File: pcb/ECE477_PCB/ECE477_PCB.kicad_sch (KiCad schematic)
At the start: 65 parts, among them J1 ESC, J2 USB_B_Micro, J3 AUX_PWR, J4 DEBUG, J5 ELRS, M1 Brushed_DC, M2 Brushed_DC, M3 Brushed_DC, M4 Brushed_DC, Q1 IRLML6244TR, Q2 IRLML6244TR, Q3 IRLML6244TR, Q4 IRLML6244TR, SW1 RESET, U1 LM78L05_TO92, U2 LM1117-3.3, U3 FT230XQ, U4 STM32F446RETx, Y1 16MHz X322516MLB4SI

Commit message: modified layout of motor control and power, added minimal initial schematic for LiDAR and footprints
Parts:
- removed U1: LM78L05_TO92, Package_TO_SOT_THT:TO-92_Inline, symbol Regulator_Linear:LM78L05_TO92
- added C10, C12, C13, C14, C8, C9: 0.1uF, Capacitor_SMD:C_0603_1608Metric, symbol Device:C_Small
- added C16, C17: 1uF, Capacitor_SMD:C_0603_1608Metric, symbol Device:C_Small
- added C29: 33uF 35V, Capacitor_SMD:C_1206_3216Metric, symbol Device:C_Small
- added D4: 5V, LED_SMD:LED_0603_1608Metric, symbol Device:LED
- added H1, H2, H3, H4: MountingHole, MountingHole:MountingHole_3.2mm_M3, symbol Mechanical:MountingHole
- added J10: ToF 5, Connector_PinHeader_1.00mm:PinHeader_1x05_P1.00mm_Vertical, symbol Connector_Generic:Conn_01x05
- added J6: ToF 1, Connector_PinHeader_1.00mm:PinHeader_1x05_P1.00mm_Vertical, symbol Connector_Generic:Conn_01x05
- added J7: ToF 2, Connector_PinHeader_1.00mm:PinHeader_1x05_P1.00mm_Vertical, symbol Connector_Generic:Conn_01x05
- added J8: ToF 3, Connector_PinHeader_1.00mm:PinHeader_1x05_P1.00mm_Vertical, symbol Connector_Generic:Conn_01x05
- added J9: ToF 4, Connector_PinHeader_1.00mm:PinHeader_1x05_P1.00mm_Vertical, symbol Connector_Generic:Conn_01x05
- added R9: 4.7k, Resistor_SMD:R_0603_1608Metric, symbol Device:R
- added U2: Pololu_S13V10F5, Connector_PinHeader_2.54mm:PinHeader_1x03_P2.54mm_Horizontal, symbol Pololu_Regulator:Pololu_S13V10F5
- D3: renamed from D1; value LED -> 3.3V
- D5: renamed from D2; value LED -> ST
- J4: renamed from J5; footprint Connector_PinHeader_2.54mm:PinHeader_1x04_P2.54mm_Vertical -> Connector_PinHeader_1.27mm:PinHeader_1x04_P1.27mm_Vertical
- TP1: footprint TestPoint:TestPoint_THTPad_D1.5mm_Drill0.7mm -> TestPoint:TestPoint_Pad_D1.0mm
- TP2: footprint (none) -> TestPoint:TestPoint_Pad_D1.0mm
- U3: renamed from U2; value LM1117-3.3 -> REG1117-3.3; footprint (none) -> Package_TO_SOT_SMD:SOT-223
- renumbered C3 to C1, C19 to C11, C18 to C15, C22 to C18, C20 to C19, C6 to C2, C21 to C20, C1 to C21, C2 to C22, C8 to C23, C17 to C24, C4 to C3, C7 to C4, C9 to C6, C10 to C7, D7 to D1, D8 to D2, D3 to D6, D4 to D7, D5 to D8, D6 to D9, J4 to J1, J1 to J3, J3 to J5, R25 to R1, R8 to R10, R4 to R11, R18 to R12, R5 to R13, R1 to R14, R9 to R15, R11 to R16, R13 to R17, R3 to R18, R10 to R19, R15 to R2, R12 to R20, R14 to R21, R16 to R3, R2 to R4, R7 to R5, R19 to R6, R6 to R7, R17 to R8, U4 to U1, U3 to U4
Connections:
- net +10V: now also C29.1, U2.3 (VI)
- net +3V3: now also C15.2, C10.1, C12.2, C13.2, C14.2, C8.1, C9.1; no longer C15.1
- net +5V: now also C16.2, D4.2 (A), U2.1 (VO)
- net GND: now also C15.1, C10.2, C12.1, C13.1, C14.1, C16.1, C17.1, C29.2, C8.2, C9.2, J10.1 (Pin_1), J6.1 (Pin_1), J7.1 (Pin_1), J8.1 (Pin_1), J9.1 (Pin_1), R9.1, U2.2 (GND); no longer C15.2
- net NRST: now also C17.2
- new net: D4.1 (K), R9.2
- new net +3.3V: J10.2 (Pin_2), J6.2 (Pin_2), J7.2 (Pin_2), J8.2 (Pin_2), J9.2 (Pin_2)
- new net TOF_1_SHTDN: J6.5 (Pin_5)
- new net TOF_2_SHTDN: J7.5 (Pin_5)
- new net TOF_3_SHTDN: J8.5 (Pin_5)
- new net TOF_4_SHTDN: J9.5 (Pin_5)
- new net TOF_5_SHTDN: J10.5 (Pin_5)
- new net TOF_SCLK: J10.3 (Pin_3), J6.3 (Pin_3), J7.3 (Pin_3), J8.3 (Pin_3), J9.3 (Pin_3)
- new net TOF_SDA: J10.4 (Pin_4), J6.4 (Pin_4), J7.4 (Pin_4), J8.4 (Pin_4), J9.4 (Pin_4)
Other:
- removed sheet DataLogger
- moved on the sheet: C11, C15, D3, D5, R10, R11, R12, R13, R4, R5, R6

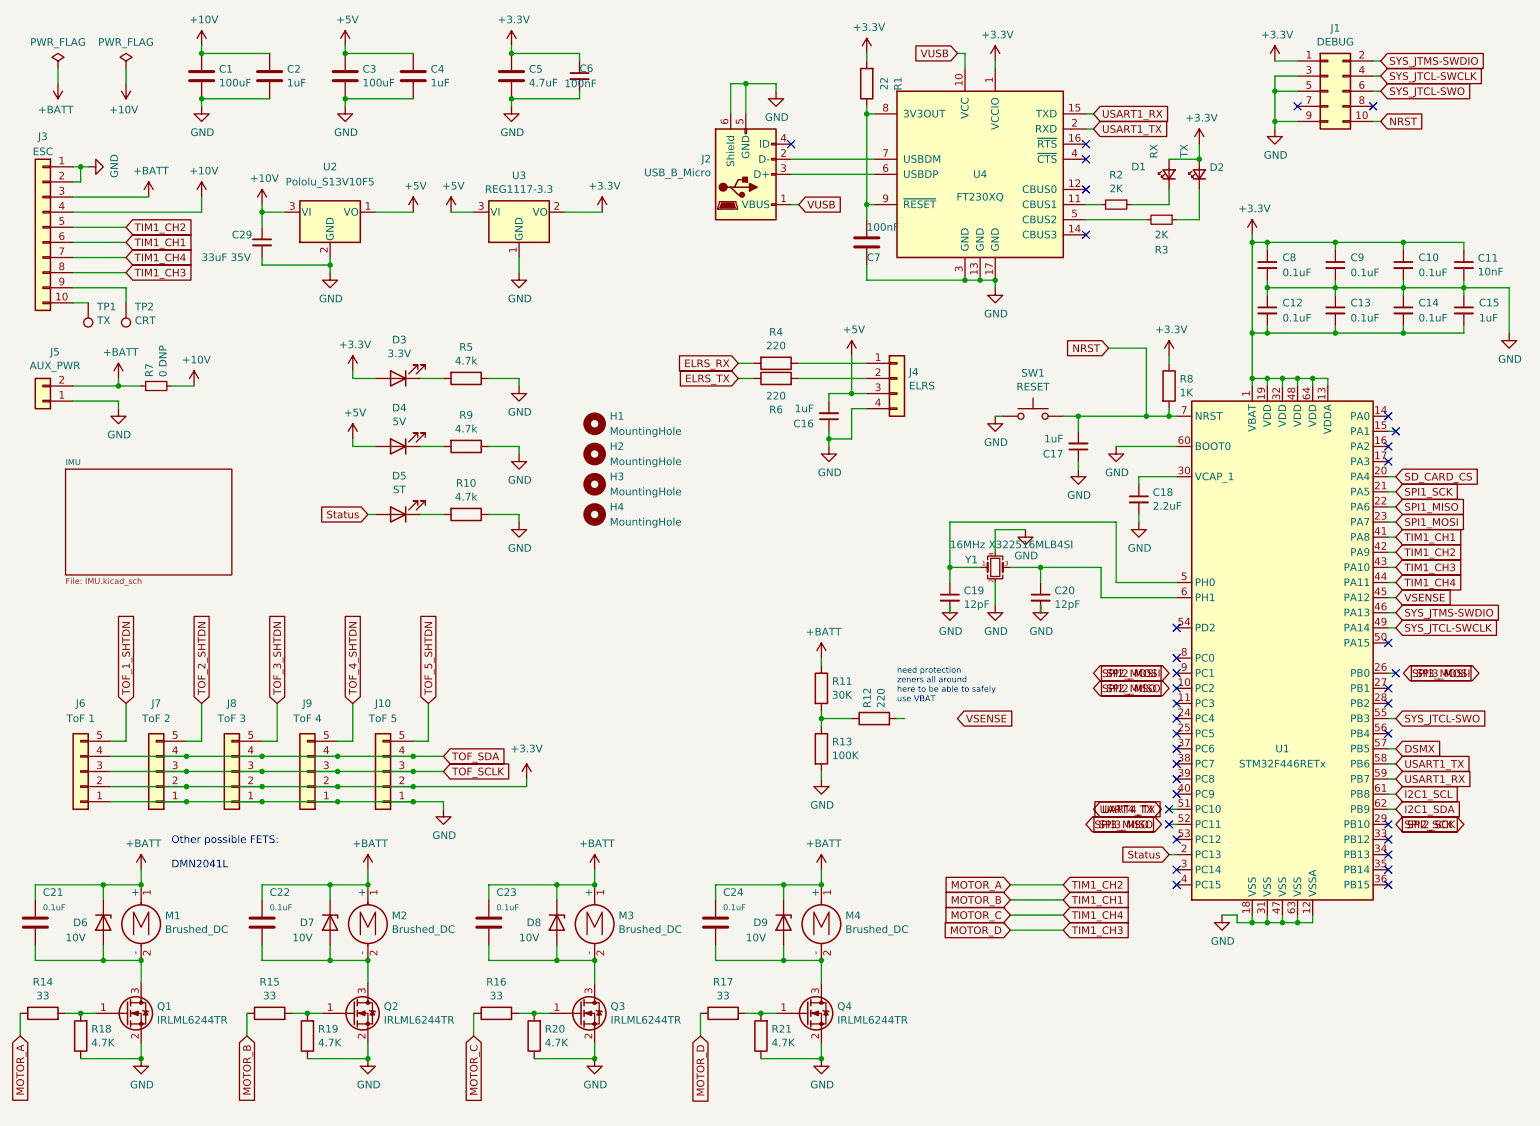
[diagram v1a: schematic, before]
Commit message: updated schematic I2C and UART connections
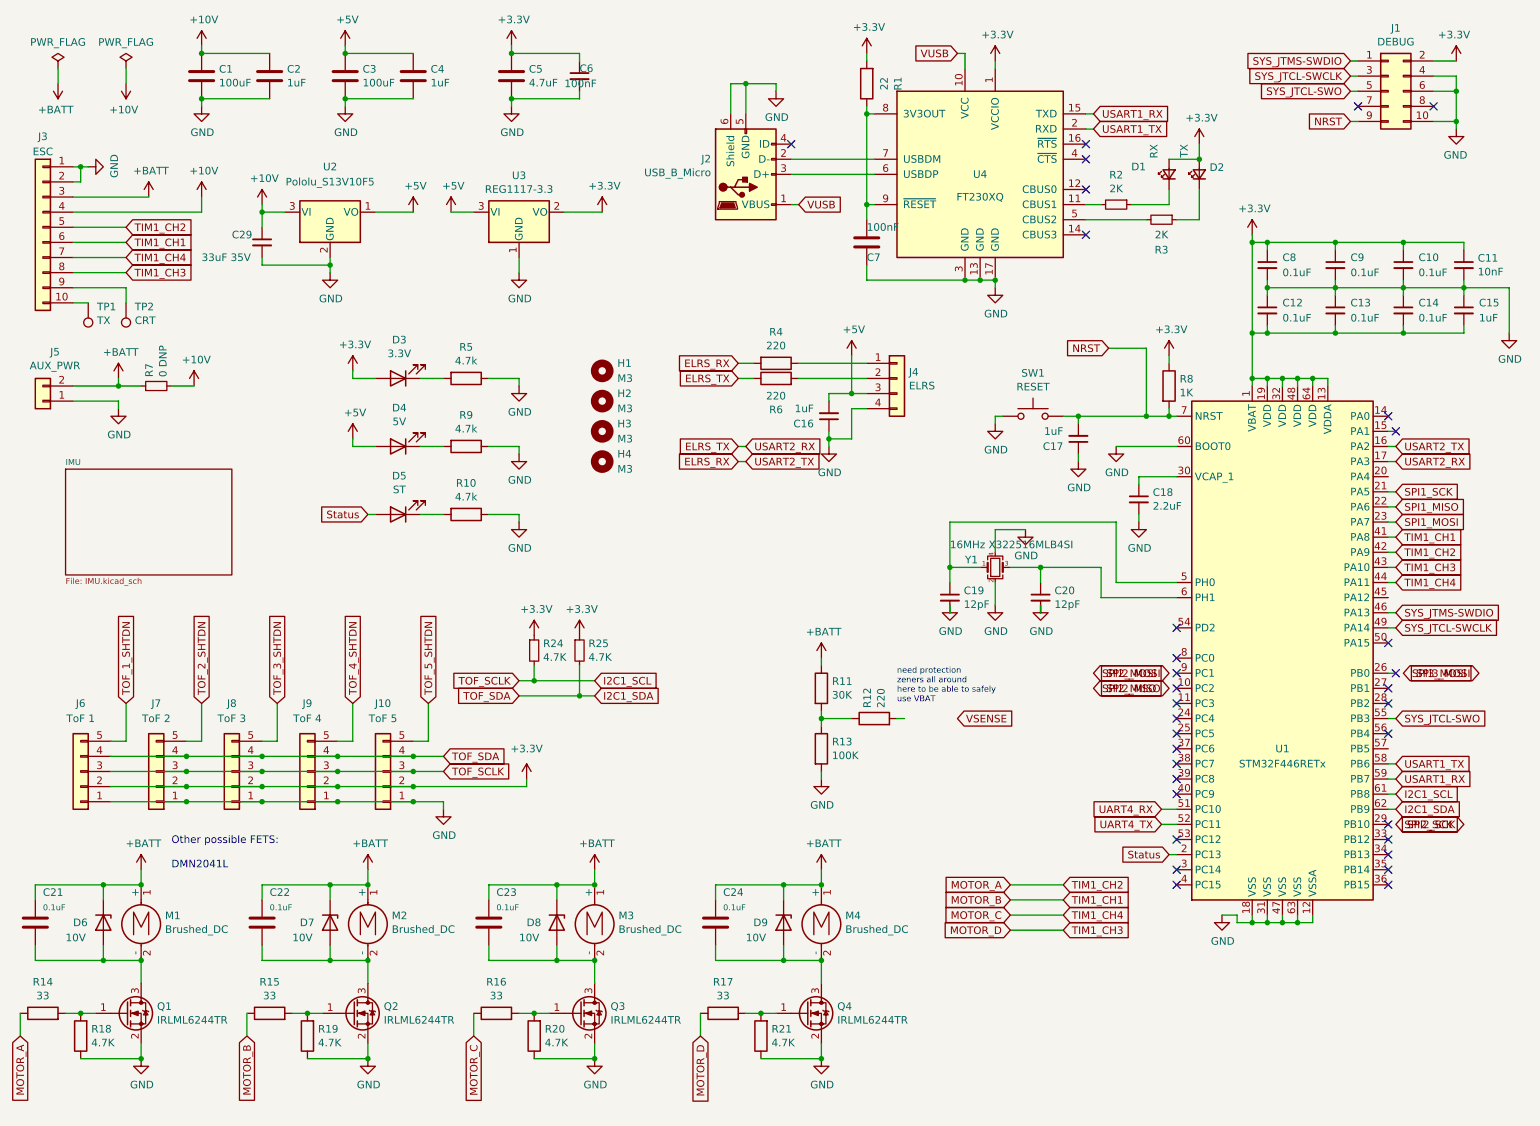
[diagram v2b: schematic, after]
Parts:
- added R24, R25: 4.7K, Resistor_SMD:R_0603_1608Metric, symbol Device:R_Small
- H1, H2, H3, H4: value MountingHole -> M3
- J2: footprint Connector_USB:USB_Micro-B_Molex_47346-0001 -> Connector_USB:USB_Micro-B_Molex-105017-0001
- J4: footprint Connector_PinHeader_1.27mm:PinHeader_1x04_P1.27mm_Vertical -> Connector_PinSocket_1.27mm:PinSocket_1x04_P1.27mm_Vertical
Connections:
- net TOF_SCLK is gone; now on net I2C1_SCL: J10.3 (Pin_3), J6.3 (Pin_3), J7.3 (Pin_3), J8.3 (Pin_3), J9.3 (Pin_3)
- net TOF_SDA is gone; now on net I2C1_SDA: J10.4 (Pin_4), J6.4 (Pin_4), J7.4 (Pin_4), J8.4 (Pin_4), J9.4 (Pin_4)
- net +3V3: now also J1.2 (Pin_2), R24.1, R25.1; no longer J1.1 (Pin_1)
- net ELRS_RX: now also U1.16 (PA2)
- net ELRS_TX: now also U1.17 (PA3)
- net GND: now also J1.10 (Pin_10), J1.4 (Pin_4), J1.6 (Pin_6); no longer J1.3 (Pin_3), J1.5 (Pin_5), J1.9 (Pin_9)
- net I2C1_SCL: now also R24.2
- net I2C1_SDA: now also R25.2
- net NRST: now also J1.9 (Pin_9); no longer J1.10 (Pin_10)
- net SYS_JTCL-SWCLK: now also J1.3 (Pin_3); no longer J1.4 (Pin_4)
- net SYS_JTCL-SWO: now also J1.5 (Pin_5); no longer J1.6 (Pin_6)
- net SYS_JTMS-SWDIO: now also J1.1 (Pin_1); no longer J1.2 (Pin_2)
- net UART4_TX: now also U1.52 (PC11)
- net VSENSE: no longer U1.45 (PA12)
- net UART4_RX: now reaches U1.51 (PC10)
- net DSMX: no longer names the net of U1.57 (PB5)
- net SD_CARD_CS: no longer names the net of U1.20 (PA4)
- no-connect marks 37 -> 33
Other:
- moved on the sheet: C17, H1, H2, H3, H4, J1

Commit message: getting pretty close. fixed DRC errors, moved UARTS and radio connector, added pi zero connector
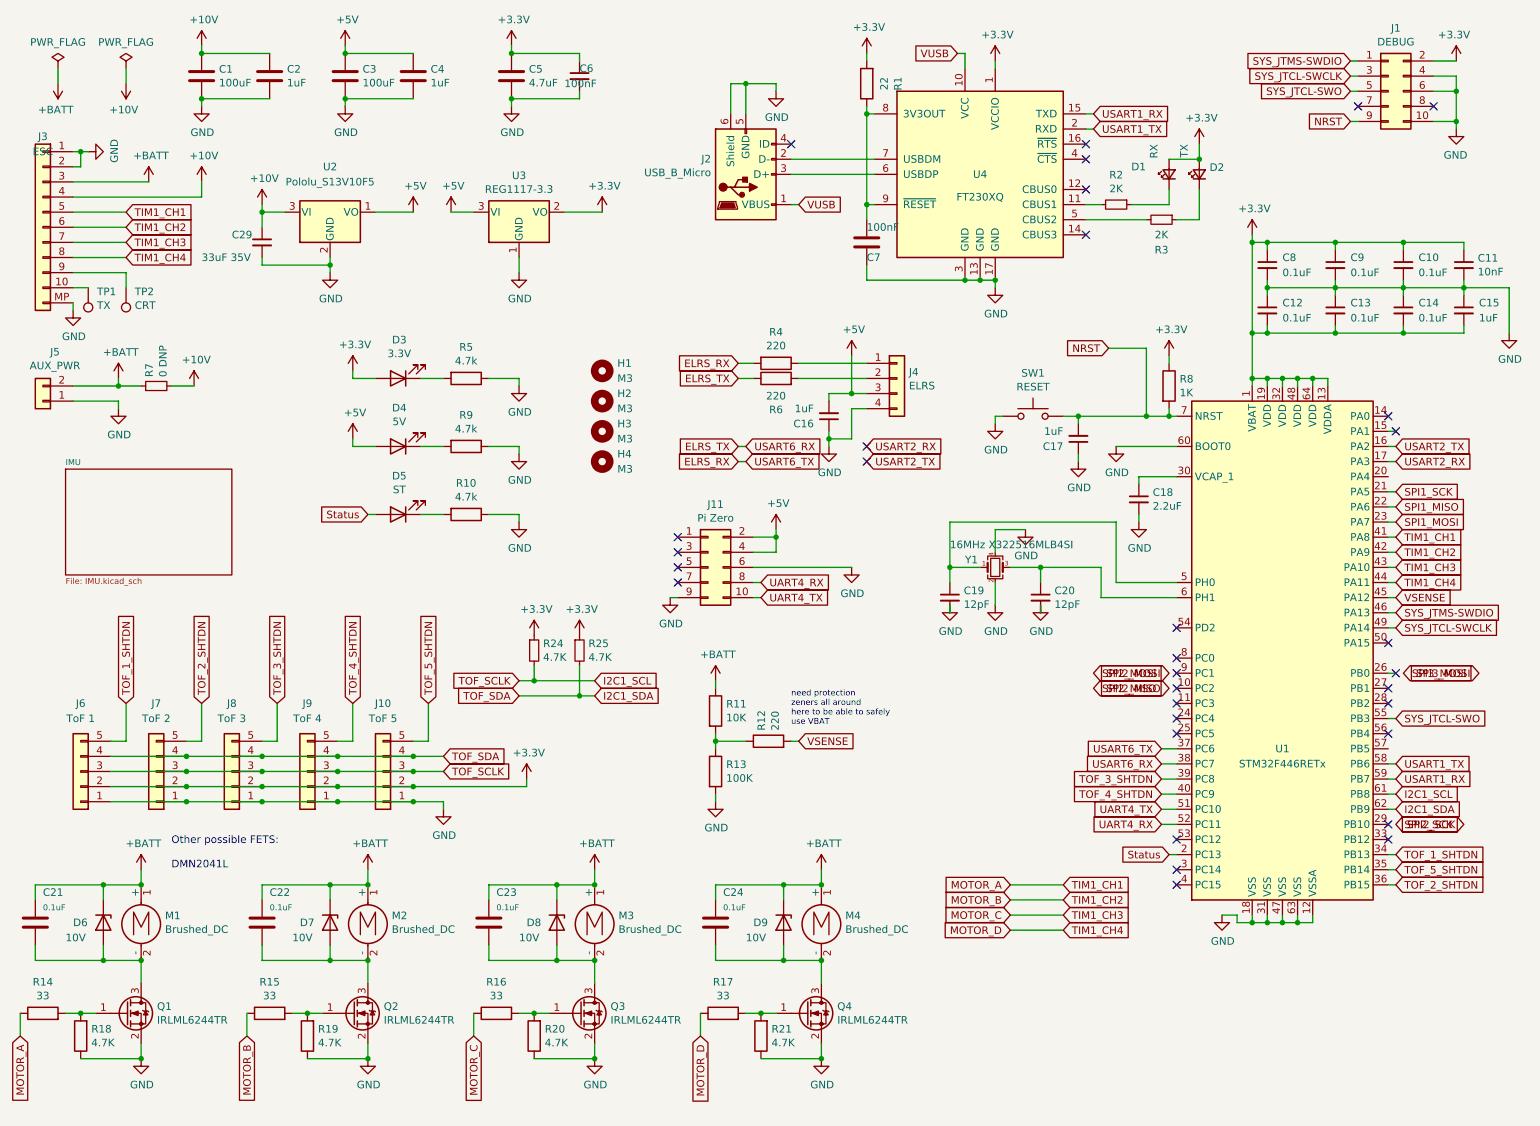
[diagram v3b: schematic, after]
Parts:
- added J11: Pi Zero, Connector_PinHeader_2.54mm:PinHeader_2x05_P2.54mm_Vertical, symbol Connector_Generic:Conn_02x05_Odd_Even
- J3: symbol Connector_Generic:Conn_01x10 -> Connector_Generic:Conn_01x11
- R11: value 30K -> 10K
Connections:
- net +3.3V is gone; now on net +3V3: J10.2 (Pin_2), J6.2 (Pin_2), J7.2 (Pin_2), J8.2 (Pin_2), J9.2 (Pin_2)
- net +5V: now also J11.2 (Pin_2), J11.4 (Pin_4)
- net ELRS_RX: now also U1.37 (PC6); no longer U1.16 (PA2)
- net ELRS_TX: now also U1.38 (PC7); no longer U1.17 (PA3)
- net GND: now also J3.MP (Pin_11), J11.6 (Pin_6), J11.9 (Pin_9)
- net MOTOR_A: now also U1.41 (PA8); no longer U1.42 (PA9)
- net MOTOR_B: now also U1.42 (PA9); no longer U1.41 (PA8)
- net MOTOR_C: now also U1.43 (PA10); no longer U1.44 (PA11)
- net MOTOR_D: now also U1.44 (PA11); no longer U1.43 (PA10)
- net TOF_1_SHTDN: now also U1.34 (PB13)
- net TOF_2_SHTDN: now also U1.36 (PB15)
- net TOF_3_SHTDN: now also U1.39 (PC8)
- net TOF_4_SHTDN: now also U1.40 (PC9)
- net TOF_5_SHTDN: now also U1.35 (PB14)
- net UART4_RX: now also U1.52 (PC11), J11.8 (Pin_8); no longer U1.51 (PC10)
- net UART4_TX: now also U1.51 (PC10), J11.10 (Pin_10); no longer U1.52 (PC11)
- net VSENSE: now also R12.2, U1.45 (PA12)
- new net USART2_RX: U1.17 (PA3)
- new net USART2_TX: U1.16 (PA2)
- no-connect marks 33 -> 32
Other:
- moved on the sheet: R11, R12, R13, TP1, TP2
